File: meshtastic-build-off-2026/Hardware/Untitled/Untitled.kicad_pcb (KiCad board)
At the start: 4 copper layers, 46 x 85 mm, 43 parts, among them J1 USB_C_Receptacle_USB2.0_16P, J2 Conn_01x02_Socket, Q1 Q_PMOS_GSD, SW1 SW_Push, SW10 SW_Push, SW11 SW_Push, SW12 SW_Push, SW13 SW_Push, SW14 SW_Push, SW15 SW_Push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

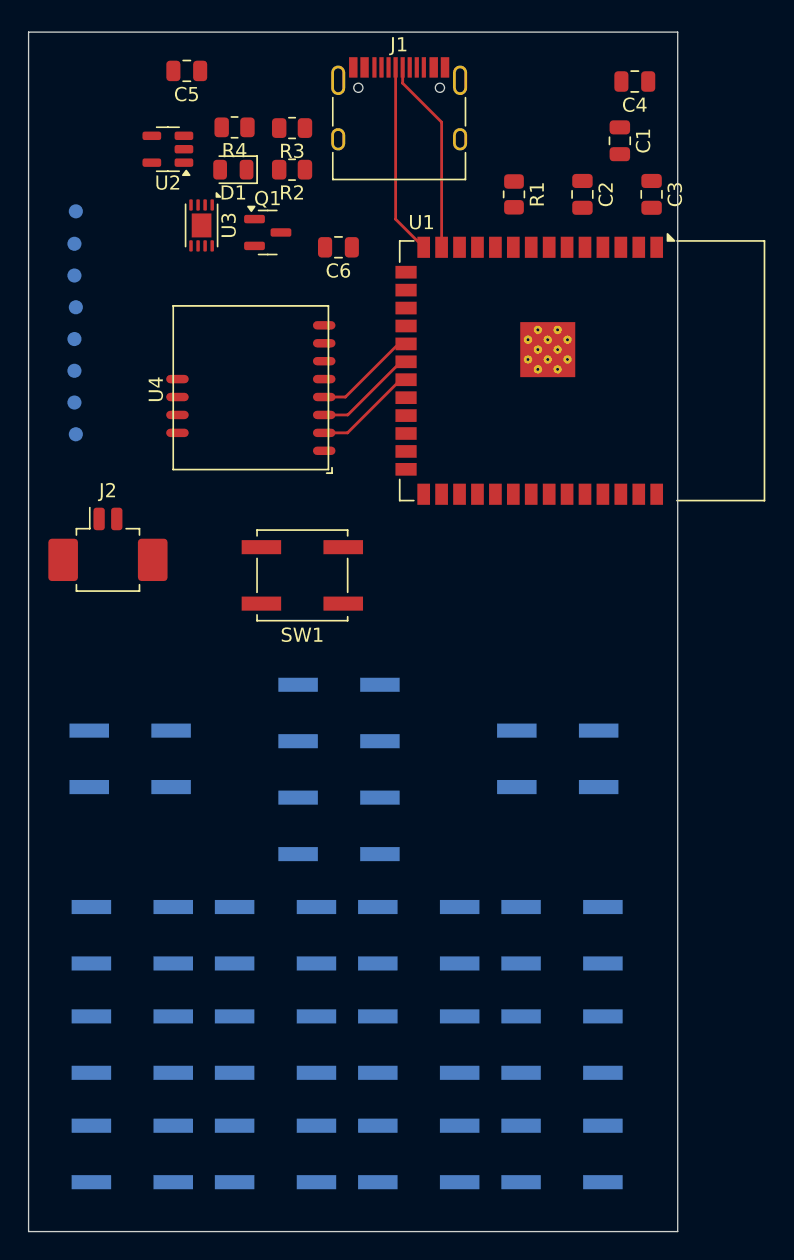
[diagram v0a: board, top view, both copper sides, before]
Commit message: Working DRC
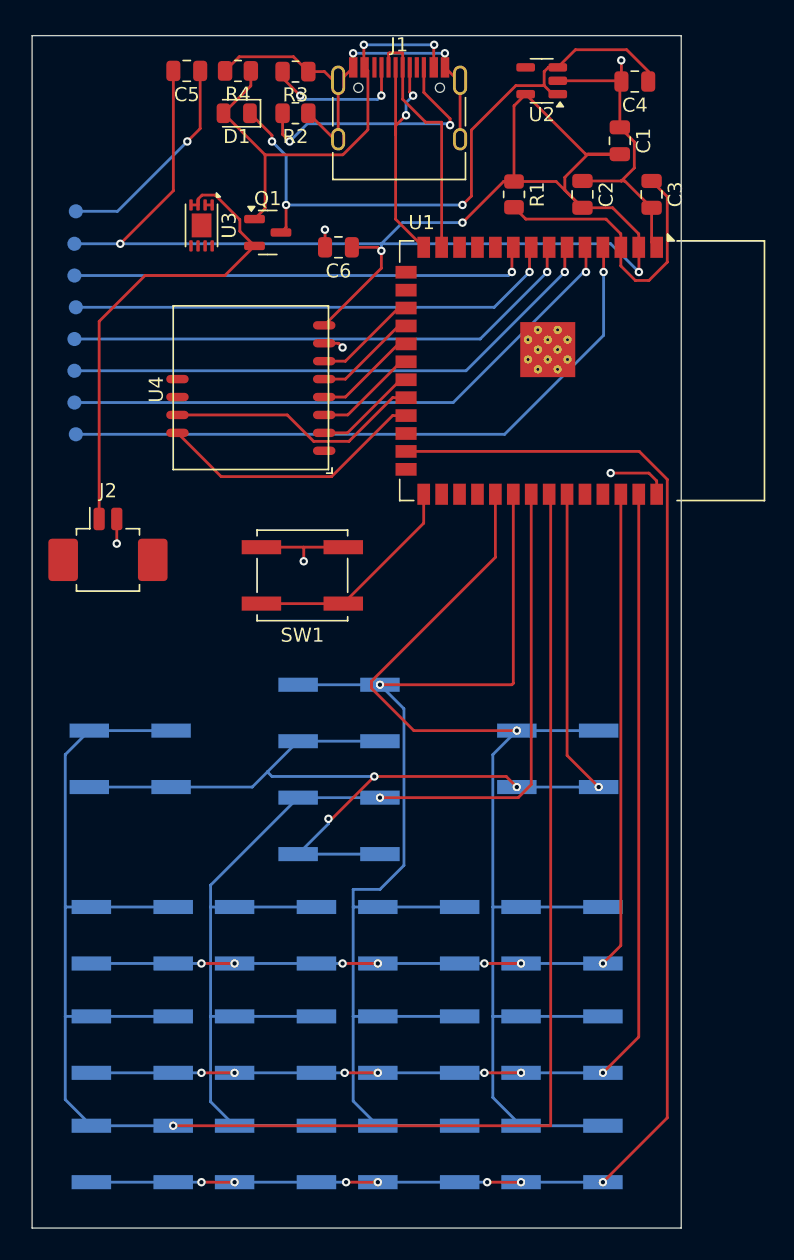
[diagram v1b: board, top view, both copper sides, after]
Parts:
- moved U2 26.9 mm to (69.9, 36.2)
- moved D1 4.01 mm to (48.2, 38.5)
- moved R2 4.01 mm to (52.4, 38.5)
- moved R3 4.01 mm to (52.4, 35.5)
- moved R4 4.01 mm to (48.3, 35.5)
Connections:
- net /LoRa_Radio/SPI_MISO renamed /LoRa_Radio/SPI_MISO_LORA
- TP5 pad 1: /LoRa_Radio/SPI_MOSI -> /MCU_Core/TFT_MOSI
- TP6 pad 1: /LoRa_Radio/SPI_SCK -> /MCU_Core/TFT_SCK
- U1 pad 17: /MCU_Core/DISPLAY_CS -> /LoRa_Radio/LORA_CS
- U1 pad 18: /LoRa_Radio/LORA_CS -> /LoRa_Radio/LORA_RST
- U1 pad 19: /LoRa_Radio/SPI_SCK -> /LoRa_Radio/SPI_SCK_LORA
- U1 pad 20: /LoRa_Radio/SPI_MOSI -> /LoRa_Radio/SPI_MOSI_LORA
- U1 pad 22: unconnected-(U1-IO14-Pad22) -> /LoRa_Radio/LORA_DI02
- U1 pad 23: /MCU_Core/KB_C2 -> /LoRa_Radio/LORA_DI01
- U1 pad 24: /MCU_Core/KB_C3 -> unconnected-(U1-IO47-Pad24)
- U1 pad 38: unconnected-(U1-IO2-Pad38) -> /MCU_Core/KB_C2
- U1 pad 39: unconnected-(U1-IO1-Pad39) -> /MCU_Core/KB_C3
- U1 pad 4: /MCU_Core/TFT_DC -> /MCU_Core/TFT_BL
- U1 pad 5: /MCU_Core/TFT_RST -> /MCU_Core/DISPLAY_CS
- U1 pad 6: /MCU_Core/TFT_BL -> /MCU_Core/TFT_DC
- U1 pad 7: /LoRa_Radio/LORA_RST -> /MCU_Core/TFT_RST
- U1 pad 8: /LoRa_Radio/LORA_DI01 -> /MCU_Core/TFT_MOSI
- U1 pad 9: /LoRa_Radio/LORA_DI02 -> /MCU_Core/TFT_SCK
- U4 pad 3: /LoRa_Radio/SPI_MOSI -> /LoRa_Radio/SPI_MOSI_LORA
- U4 pad 4: /LoRa_Radio/SPI_SCK -> /LoRa_Radio/SPI_SCK_LORA
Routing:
- net /MCU_Core/KB_R4: track 0.00 -> 127.9 mm, vias 0 -> 1
- net +3V3: track 0.00 -> 110.8 mm, vias 0 -> 4
- net /MCU_Core/KB_C4: track 0.00 -> 107.3 mm, vias 0 -> 7
- net /MCU_Core/KB_R1: track 0.00 -> 85.7 mm, vias 0 -> 1
- net /MCU_Core/KB_R2: track 0.00 -> 84.9 mm, vias 0 -> 1
- net /MCU_Core/KB_R3: track 0.00 -> 84.8 mm, vias 0 -> 1
- net /MCU_Core/KB_C1: track 0.00 -> 81.2 mm, vias 0 -> 4
- net /MCU_Core/KB_C3: track 0.00 -> 78.3 mm, vias 0 -> 7
- net /MCU_Core/KB_C2: track 0.00 -> 70.0 mm, vias 0 -> 7
- net GND: track 0.00 -> 53.6 mm, vias 0 -> 7
- net /MCU_Core/TFT_BL: track 0.00 -> 46.6 mm, vias 0 -> 1
- net /Power_Management/V_SYS: track 0.00 -> 45.8 mm, vias 0 -> 3
- net /MCU_Core/DISPLAY_CS: track 0.00 -> 41.9 mm, vias 0 -> 1
- net /MCU_Core/TFT_DC: track 0.00 -> 39.5 mm, vias 0 -> 1
- net /MCU_Core/TFT_RST: track 0.00 -> 37.3 mm, vias 0 -> 1
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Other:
- board size 46 x 85 mm -> 46 x 84.5 mm

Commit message: For Review
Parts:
- added NA: LOGO, LOGO, F.Cu at (56.6, 114.5)
- moved SW2 0.35 mm to (71.3, 84.2)
- moved SW14 0.20 mm to (40.9, 84.2)
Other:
- board size 46 x 84.5 mm -> 45.8 x 85 mm

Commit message: updated PCB
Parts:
- removed NA: LOGO, LOGO
- added G***: LOGO, LOGO, F.Cu at (77.0, 89.2)
- SW1, SW10, SW11, SW12, SW13, SW14, SW15, SW16, SW17, SW2, SW3, SW4, SW5, SW6, SW7, SW8, SW9: footprint Button_Switch_SMD:SW_Push_1P1T_NO_CK_KSC6xxJ -> Button_Switch_SMD:SW_SPST_Omron_B3FS-100xP
- moved SW5 43.5 mm to (41.2, 80.8)
- moved SW14 38.5 mm to (72.0, 107.0)
- moved SW4 30.9 mm to (51.5, 80.8)
- moved SW9 30.2 mm to (41.2, 89.5)
- moved SW15 23.3 mm to (61.8, 107.0)
- moved SW10 18.9 mm to (72.0, 98.2)
- moved SW3 18.6 mm to (61.8, 80.8)
- moved SW6 18.6 mm to (72.0, 89.5)
- moved SW8 17.8 mm to (51.5, 89.5)
- moved U4 17.2 mm to (43.8, 50.6), turned to -90 degrees
- moved SW13 17.1 mm to (41.2, 98.2)
- moved SW16 10.9 mm to (51.5, 107.0)
- moved SW11 10.9 mm to (61.8, 98.2)
- moved SW7 7.27 mm to (61.8, 89.5)
- moved SW12 6.27 mm to (51.5, 98.2)
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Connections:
- U1 pad 17: /LoRa_Radio/LORA_CS -> /LoRa_Radio/LORA_DI01
- U1 pad 18: /LoRa_Radio/LORA_RST -> /LoRa_Radio/LORA_DI02
- U1 pad 19: /LoRa_Radio/SPI_SCK_LORA -> /LoRa_Radio/SPI_MISO_LORA
- U1 pad 21: /LoRa_Radio/SPI_MISO_LORA -> /LoRa_Radio/SPI_SCK_LORA
- U1 pad 22: /LoRa_Radio/LORA_DI02 -> /LoRa_Radio/LORA_RST
- U1 pad 23: /LoRa_Radio/LORA_DI01 -> /LoRa_Radio/LORA_CS
- U1 pad 25: /MCU_Core/KB_C4 -> /MCU_Core/KB_C1
- U1 pad 35: /MCU_Core/KB_C1 -> /MCU_Core/KB_C4
- U1 pad 38: /MCU_Core/KB_C2 -> /MCU_Core/KB_C3
- U1 pad 39: /MCU_Core/KB_C3 -> /MCU_Core/KB_C2
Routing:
- net /MCU_Core/KB_R4: track 127.9 -> 104.8 mm, vias 1 -> 7
- net /MCU_Core/KB_C2: track 70.0 -> 92.3 mm, vias 7 -> 1
- net +3V3: track 110.8 -> 90.7 mm, vias 4 -> 7
- net /MCU_Core/KB_C3: track 78.3 -> 93.5 mm, vias 7 -> 1
- net /LoRa_Radio/LORA_DI01: track 19.3 -> 6.16 mm
- net GND: track 53.6 -> 40.8 mm, vias 7 -> 12
- net /LoRa_Radio/LORA_DI02: track 18.3 -> 6.16 mm
- net /MCU_Core/KB_R3: track 84.8 -> 95.3 mm, vias 1 -> 7
- net /LoRa_Radio/SPI_MISO_LORA: track 7.36 -> 17.6 mm
- net /LoRa_Radio/SPI_MOSI_LORA: track 7.36 -> 17.6 mm
- net /LoRa_Radio/SPI_SCK_LORA: track 7.36 -> 17.6 mm
- net /LoRa_Radio/LORA_RST: track 7.36 -> 16.9 mm
- net /LoRa_Radio/LORA_CS: track 7.36 -> 16.9 mm
- net /MCU_Core/KB_C1: track 81.2 -> 90.4 mm, vias 4 -> 1
- net /MCU_Core/KB_R1: track 85.7 -> 77.0 mm
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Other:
- board size 45.8 x 85 mm -> 45.8 x 79.2 mm

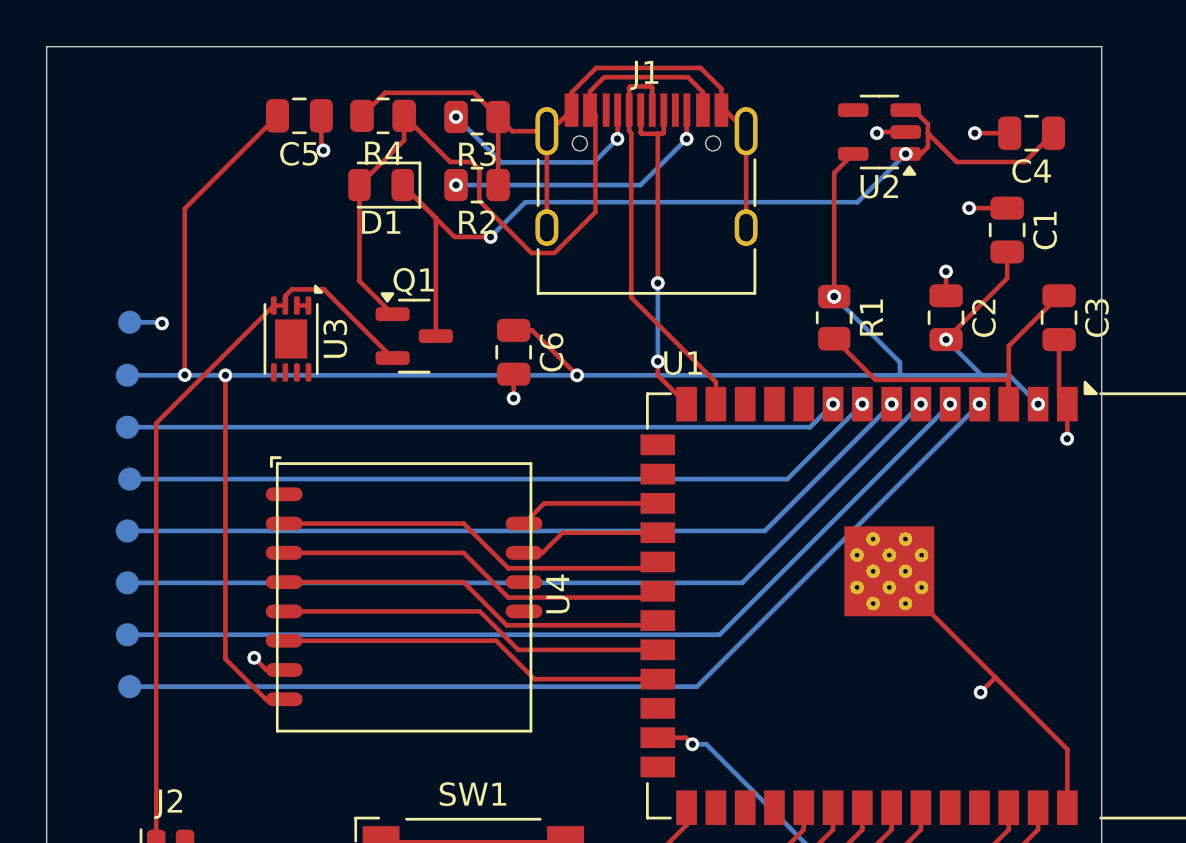
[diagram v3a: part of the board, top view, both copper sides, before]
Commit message: update power rails and vias width
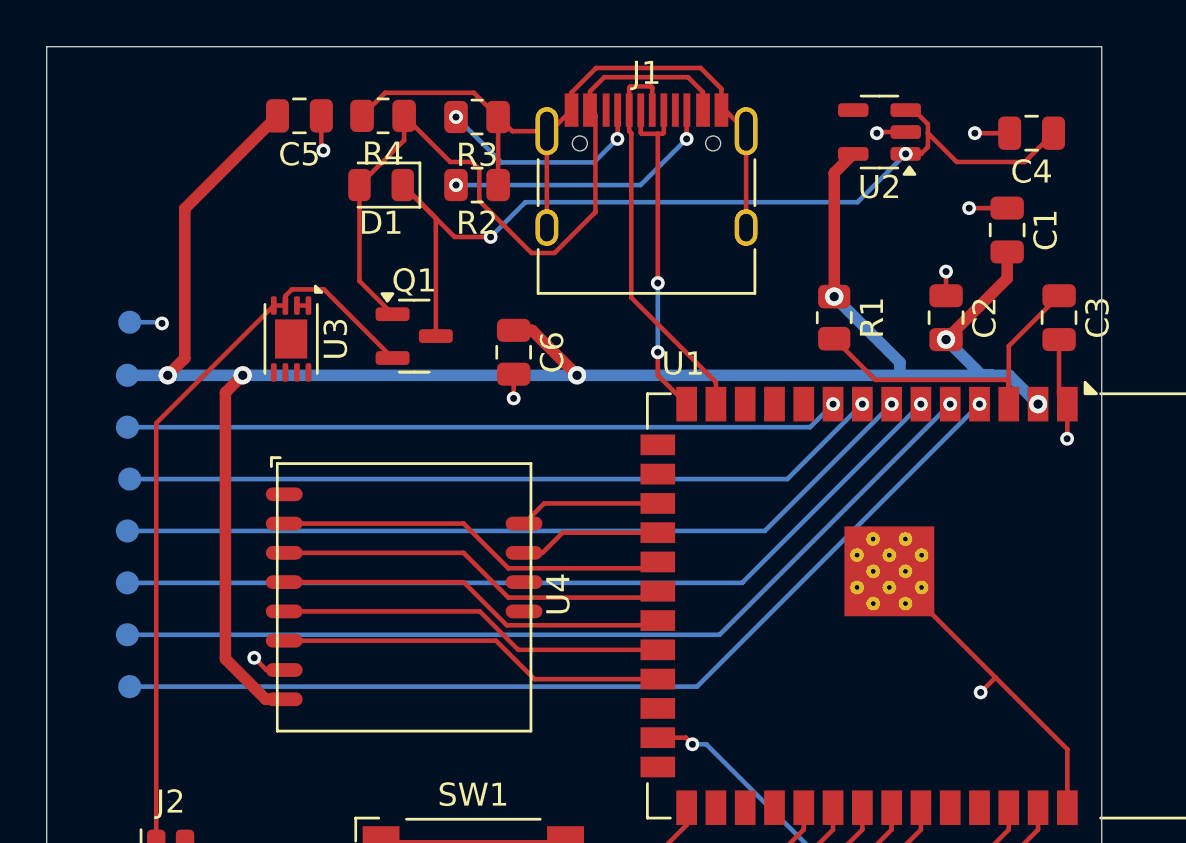
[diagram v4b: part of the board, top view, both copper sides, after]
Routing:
- net +3V3: track 90.7 -> 91.3 mm, vias 7 -> 6
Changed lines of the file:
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@@
+	)
+	(segment
+		(start 43.250001 60.79875)
+		(end 44.05 60.79875)
+		(width 0.5)
+		(layer "F.Cu")
+		(net 1)
 	)
 	(segment
 		(start 67.9 43.3375)
 		(end 67.9 37.975)
-		(width 0.2)
+		(width 0.5)
+		(layer "F.Cu")
+		(net 1)
+	)
+	(segment
+		(start 41.5 59.048749)
+		(end 43.250001 60.79875)
+		(width 0.5)
+		(layer "F.Cu")
+		(net 1)
+	)
+	(segment
+		(start 42.25 46.75)
+		(end 41.5 47.5)
+		(width 0.5)
+		(layer "F.Cu")
+		(net 1)
+	)
+	(segment
+		(start 39.738235 39.521765)
+		(end 43.76 35.5)
+		(width 0.5)
 		(layer "F.Cu")
 		(net 1)
@@
 		(start 67.9 37.975)
 		(end 68.725 37.15)
-		(width 0.2)
-		(layer "F.Cu")
-		(net 1)
-	)
-	(segment
-		(start 44.05 60.79875)
-		(end 43.250001 60.79875)
-		(width 0.2)
+		(width 0.5)
+		(layer "F.Cu")
+		(net 1)
+	)
+	(segment
+		(start 41.5 47.5)
+		(end 41.5 59.048749)
+		(width 0.5)
 		(layer "F.Cu")
 		(net 1)
@@
 		(start 75.4 42.55)
 		(end 72.75 45.2)
-		(width 0.2)
-		(layer "F.Cu")
-		(net 1)
-	)
-	(segment
-		(start 41.5 59.048749)
-		(end 41.5 46.75)
-		(width 0.2)
+		(width 0.5)
 		(layer "F.Cu")
 		(net 1)
@@
 		(start 75.4 41.4)
 		(end 75.4 42.55)
-		(width 0.2)
+		(width 0.5)
 		(layer "F.Cu")
 		(net 1)
@@
 		(start 54 44.8)
 		(end 54.8 44.8)
-		(width 0.2)
-		(layer "F.Cu")
-		(net 1)
-	)
-	(segment
-		(start 43.76 35.5)
-		(end 39.738235 39.521765)
-		(width 0.2)
+		(width 0.5)
 		(layer "F.Cu")
 		(net 1)
@@
 		(start 54.8 44.8)
 		(end 56.75 46.75)
-		(width 0.2)
-		(layer "F.Cu")
-		(net 1)
-	)
-	(segment
-		(start 43.250001 60.79875)
-		(end 41.5 59.048749)
-		(width 0.2)
-		(layer "F.Cu")
-		(net 1)
-	)
-	(segment
-		(start 39.738235 39.521765)
-		(end 39.738235 46.738235)
-		(width 0.2)
+		(width 0.5)
+		(layer "F.Cu")
+		(net 1)
+	)
+	(segment
+		(start 39 46.75)
+		(end 39.738235 46.011765)
+		(width 0.5)
+		(layer "F.Cu")
+		(net 1)
+	)
+	(segment
+		(start 39.738235 46.011765)
+		(end 39.738235 39.521765)
+		(width 0.5)
 		(layer "F.Cu")
 		(net 1)
@@
 	(via
 		(at 56.75 46.75)
-		(size 0.6)
-		(drill 0.3)
+		(size 0.8)
+		(drill 0.4)
+		(layers "F.Cu" "B.Cu")
+		(net 1)
+	)
+	(via
+		(at 39 46.75)
+		(size 0.8)
+		(drill 0.4)
+		(layers "F.Cu" "B.Cu")
+		(net 1)
+	)
+	(via
+		(at 42.25 46.75)
+		(size 0.8)
+		(drill 0.4)
+		(layers "F.Cu" "B.Cu")
+		(net 1)
+	)
+	(via
+		(at 72.75 45.2)
+		(size 0.8)
+		(drill 0.4)
 		(layers "F.Cu" "B.Cu")
 		(net 1)
@@
 	(via
 		(at 67.9 43.3375)
-		(size 0.6)
-		(drill 0.3)
-		(layers "F.Cu" "B.Cu")
-		(net 1)
-	)
-	(via
-		(at 39.738235 46.738235)
-		(size 0.6)
-		(drill 0.3)
-		(layers "F.Cu" "B.Cu")
-		(net 1)
-	)
-	(via
-		(at 41.5 46.75)
-		(size 0.6)
-		(drill 0.3)
-		(layers "F.Cu" "B.Cu")
-		(net 1)
-	)
-	(via
-		(at 72.75 45.2)
-		(size 0.6)
-		(drill 0.3)
-		(layers "F.Cu" "B.Cu")
-		(net 1)
-	)
-	(via
-		(at 67.9 43.3375)
-		(size 0.6)
-		(drill 0.3)
+		(size 0.8)
+		(drill 0.4)
 		(layers "F.Cu" "B.Cu")
 		(net 1)
@@
 	(via
 		(at 76.74 48)
-		(size 0.6)
-		(drill 0.3)
+		(size 0.8)
+		(drill 0.4)
 		(layers "F.Cu" "B.Cu")
 		(net 1)
@@
 		(start 70.75 46.75)
 		(end 74.75 46.75)
-		(width 0.2)
-		(layer "B.Cu")
-		(net 1)
-	)
-	(segment
-		(start 37.25 46.75)
-		(end 41.5 46.75)
-		(width 0.2)
+		(width 0.5)
 		(layer "B.Cu")
 		(net 1)
@@
 		(start 74.75 46.75)
 		(end 74.3 46.75)
-		(width 0.2)
+		(width 0.5)
 		(layer "B.Cu")
 		(net 1)
@@
 		(start 56.75 46.75)
 		(end 70.75 46.75)
-		(width 0.2)
+		(width 0.5)
+		(layer "B.Cu")
+		(net 1)
+	)
+	(segment
+		(start 37.25 46.75)
+		(end 42.25 46.75)
+		(width 0.5)
 		(layer "B.Cu")
 		(net 1)
@@
 		(start 74.75 46.75)
 		(end 75.49 46.75)
-		(width 0.2)
+		(width 0.5)
 		(layer "B.Cu")
 		(net 1)
@@
 		(start 70.75 46.75)
 		(end 70.75 46.1875)
-		(width 0.2)
-		(layer "B.Cu")
-		(net 1)
-	)
-	(segment
-		(start 41.5 46.75)
-		(end 56.75 46.75)
-		(width 0.2)
+		(width 0.5)
 		(layer "B.Cu")
 		(net 1)
@@
 		(start 70.75 46.1875)
 		(end 67.9 43.3375)
-		(width 0.2)
+		(width 0.5)
 		(layer "B.Cu")
 		(net 1)
@@
 		(start 75.49 46.75)
 		(end 76.74 48)
-		(width 0.2)
+		(width 0.5)
+		(layer "B.Cu")
+		(net 1)
+	)
+	(segment
+		(start 42.25 46.75)
+		(end 56.75 46.75)
+		(width 0.5)
 		(layer "B.Cu")
 		(net 1)
@@
 		(start 74.3 46.75)
 		(end 72.75 45.2)
-		(width 0.2)
+		(width 0.5)
 		(layer "B.Cu")
 		(net 1)
@@
 	)
 	(segment
-		(start 60.25 46.15)
-		(end 60.25 46.75)
-		(width 0.2)
-		(layer "F.Cu")
-		(net 11)
-	)
-	(segment
 		(start 59.51 36.227)
 		(end 59.559 36.276)
@@
 	)
 	(segment
+		(start 60.25 45.75)
+		(end 60.25 46.75)
+		(width 0.2)
+		(layer "F.Cu")
+		(net 11)
+	)
+	(segment
+		(start 60.51 36.227)
+		(end 60.51 35.25)
+		(width 0.2)
+		(layer "F.Cu")
+		(net 11)
+	)
+	(segment
 		(start 60.25 46.75)
 		(end 61.5 48)
@@
 		(net 11)
 	)
-	(segment
-		(start 60.51 36.227)
-		(end 60.51 35.25)
-		(width 0.2)
-		(layer "F.Cu")
+	(via
+		(at 60.25 42.75)
+		(size 0.6)
+		(drill 0.3)
+		(layers "F.Cu" "B.Cu")
 		(net 11)
 	)
 	(via
-		(at 60.25 42.75)
+		(at 60.25 45.75)
 		(size 0.6)
 		(drill 0.3)
@@
 		(net 11)
 	)
-	(via
-		(at 60.25 46.15)
-		(size 0.6)
-		(drill 0.3)
-		(layers "F.Cu" "B.Cu")
-		(net 11)
-	)
 	(segment
 		(start 60.25 42.75)
-		(end 60.25 46.15)
-		(width 0.2)
-		(layer "B.Cu")
+		(end 60.25 45.75)
+		(width 0.2)
+		(layer "B.Cu")
